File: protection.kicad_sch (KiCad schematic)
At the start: 43 parts, among them K1 Relay_SPDT, Q1 BSS138, Q2 BSS138, SW1 SW_Push, U10 ADR4525, U11 74LVC1G32, U3 74LVC1G10, U4 LM339, U5 74LVC1G02, U6 74LVC1G32, U7 74LVC1G02, U8 74LVC1G02, U9 TPS3823-33DBV

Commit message: can transceiver; power; mcu
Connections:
- net +3.3V: now also R11.2, R12.1
- net WDT_H: now also U6.2
- net at U4.14: now also R12.2, U6.1; no longer R12.1
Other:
- moved on the sheet: C10, C11, C12, C13, C14, C15, C16, C17, C18, C7, C8, C9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

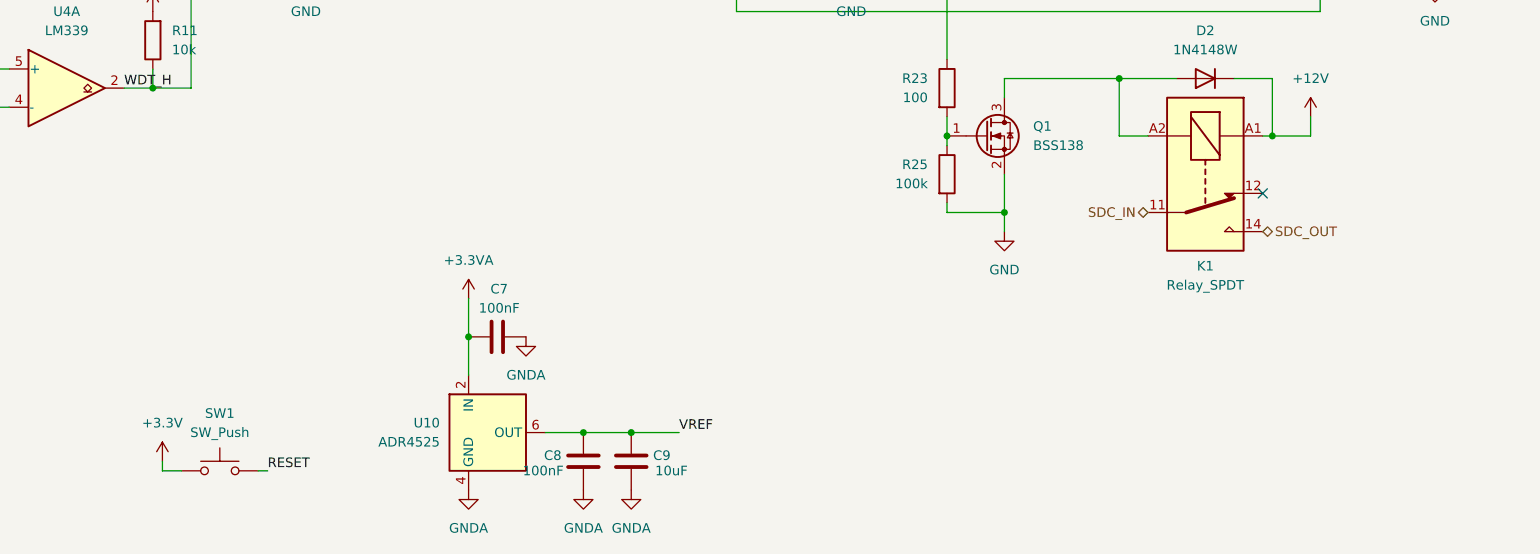
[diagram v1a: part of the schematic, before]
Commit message: Add presentation (slides, PDF, pptx) and latest schematic edits
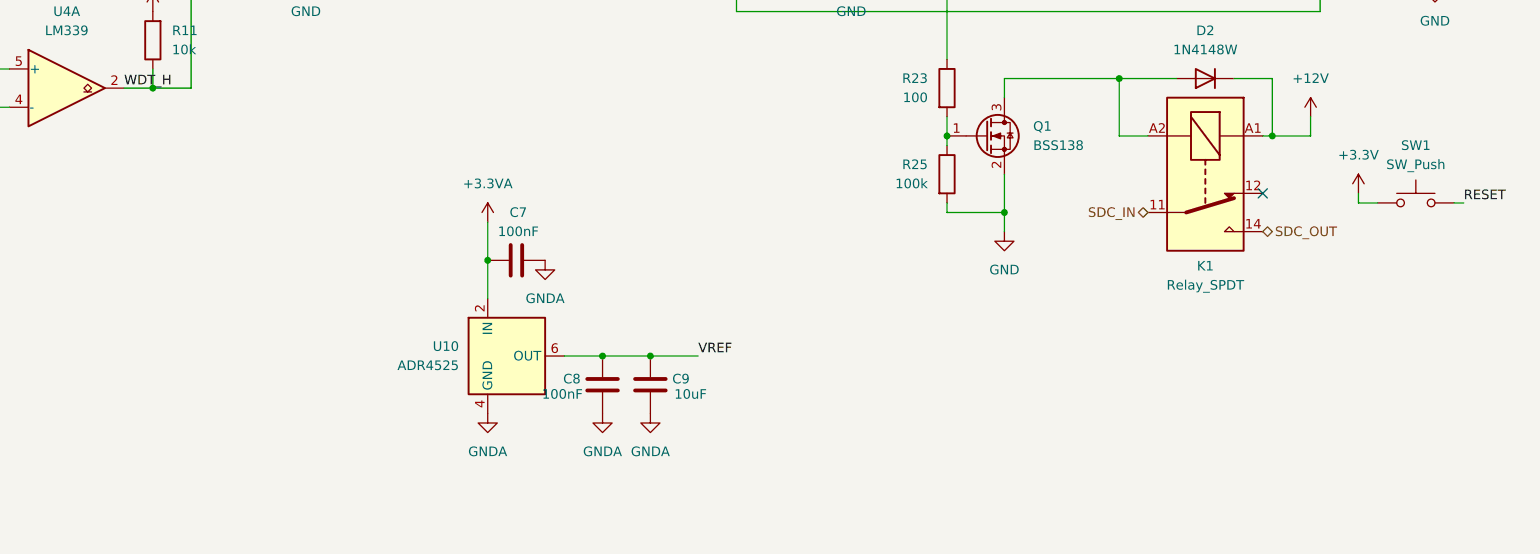
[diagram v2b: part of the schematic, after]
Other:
- moved on the sheet: C7, C8, C9, SW1, U10
